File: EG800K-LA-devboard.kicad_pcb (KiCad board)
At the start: 4 copper layers, 35 x 35 mm, 49 parts, among them J1 U.FL-R-SMT_10_, J2 MICROQTJ, J5 Conn_01x08_Pin, Q1 DTC143ZUAT106, Q2 DTC143ZUAT106, Q4 DTC143ZUAT106, Q5 DTC143ZUAT106, Q6 BSS138, Q7 BSS138, Q8 BSS138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

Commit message: version final
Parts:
- removed the G*** at (151.1, 70.5)
- added G***: LOGO, Images:LOGOv3.4, F.Cu at (166.6, 88.8)
- moved J1 2.36 mm to (149.5, 65.0)
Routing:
- net /RF_ANT: track 6.12 -> 3.76 mm
- net GND: vias 729 -> 25

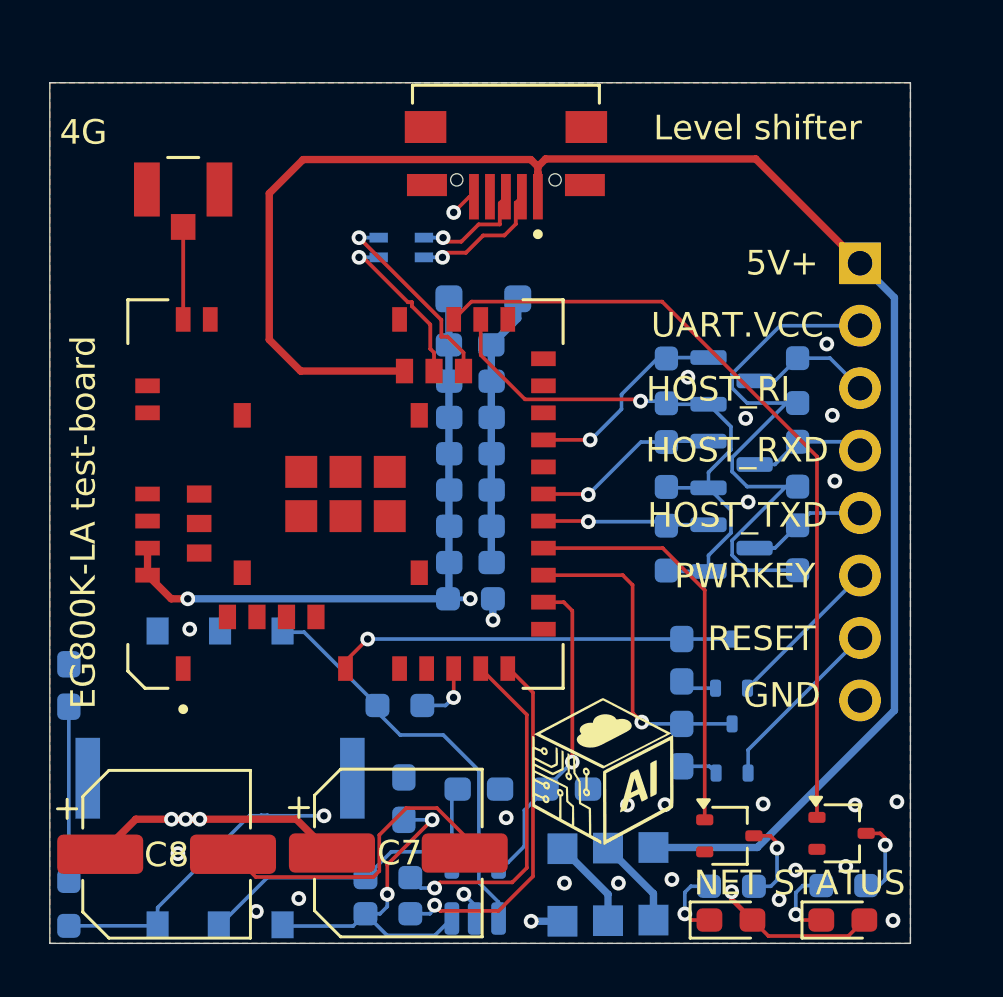
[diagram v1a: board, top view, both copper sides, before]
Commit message: cambio stack JLC PCB, cambio USB route
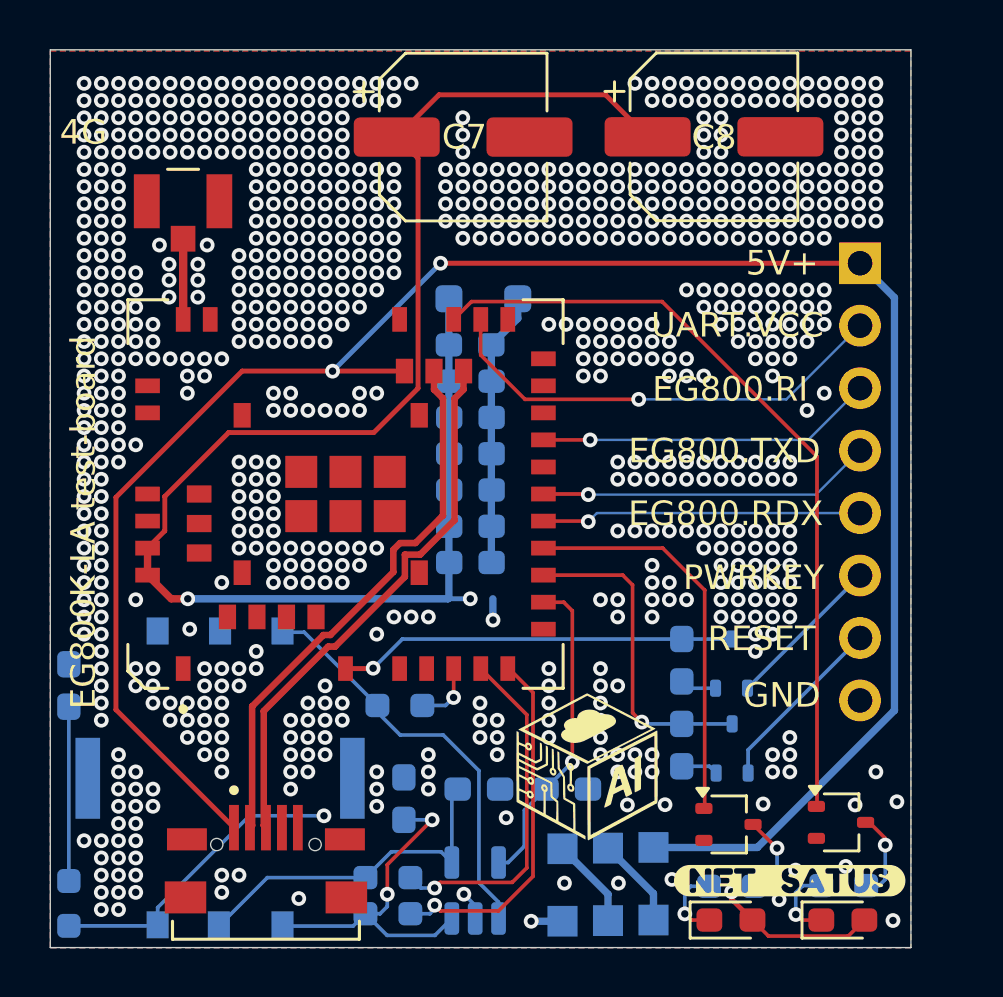
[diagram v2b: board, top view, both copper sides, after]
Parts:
- removed FL2: Choke_CommonMode_FerriteCore_1243, EasyEDA:FILTER-SMD_4P-L2.0-W1.2-BL_DLW21H
- removed Q6, Q7, Q8: BSS138, Package_TO_SOT_SMD:SOT-23
- removed R12, R13, R14, R18, R19, R20: 10k, Resistor_SMD:R_0603_1608Metric_Pad0.98x0.95mm_HandSolder
- removed R15: 0, Resistor_SMD:R_0603_1608Metric_Pad0.98x0.95mm_HandSolder
- added kibuzzard-69C732A2: G***, kibuzzard-69C732A2, F.Cu at (174.2, 93.1)
- moved C8 36.7 mm to (171.1, 62.9)
- moved C7 29.2 mm to (160.9, 62.9)
- moved J2 28.7 mm to (152.9, 91.6), turned to 0 degrees
- moved G*** 0.67 mm to (165.9, 88.6)
- moved J1 0.48 mm to (149.5, 65.5)
- moved Q5 0.46 mm to (171.7, 90.8)
- moved Q4 0.45 mm to (176.3, 90.7)
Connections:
- C21 pad 2: /EG800K.VBAT -> /DC 3.8v supply
- C22 pad 2: /EG800K.VBAT -> /DC 3.8v supply
- C23 pad 2: /EG800K.VBAT -> /DC 3.8v supply
- C24 pad 2: /EG800K.VBAT -> /DC 3.8v supply
- C25 pad 2: /EG800K.VBAT -> /DC 3.8v supply
- C26 pad 2: /EG800K.VBAT -> /DC 3.8v supply
- C27 pad 2: /EG800K.VBAT -> /DC 3.8v supply
- D5 pad 1: /EG800K.VBAT -> /DC 3.8v supply
- D6 pad 2: /EG800K.VBAT -> /DC 3.8v supply
- D7 pad 2: /EG800K.VBAT -> /DC 3.8v supply
- J2 pad 2: Net-(J2-D-) -> /EG800K.USB_D-
- J2 pad 3: Net-(J2-D+) -> /EG800K.USB_D+
- J5 pad 2: /UART.VCC -> /EG800K.VDD_ETX
- J5 pad 3: /HOST.RI_INT -> /EG800K.UART1_Ri
- J5 pad 4: /HOST_UART0_RXD -> /EG800K.UART1_TXD
- J5 pad 5: /HOST_UART0_TXD -> /EG800K.UART1_RXD
- U4 pad 42: /EG800K.VBAT -> /DC 3.8v supply
- U4 pad 43: /EG800K.VBAT -> /DC 3.8v supply
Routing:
- net /DC 3.8v supply: track 49.4 -> 127.5 mm
- net /EG800K.VBAT: track 52.1 -> 0.00 mm, vias 3 -> 0
- net /UART.VCC: track 23.7 -> 0.00 mm
- net /EG800K.USB_D-: track 6.88 -> 22.5 mm, vias 1 -> 0
- net /EG800K.USB_D+: track 8.13 -> 22.5 mm, vias 1 -> 0
- net GND: track 29.4 -> 15.4 mm, vias 25 -> 767
- net +5V: track 71.7 -> 83.4 mm, vias 0 -> 2
- net /EG800K.UART1_TXD: track 7.62 -> 14.1 mm
- net /EG800K.UART1_RXD: track 6.81 -> 13.0 mm
- net Net-(J2-D-): track 5.65 -> 0.00 mm, vias 1 -> 0
- net /EG800K.UART1_Ri: track 8.45 -> 13.8 mm
- net /HOST.RI_INT: track 5.18 -> 0.00 mm
- net /HOST_UART0_TXD: track 4.88 -> 0.00 mm
- net /HOST_UART0_RXD: track 4.82 -> 0.00 mm
- net Net-(J2-D+): track 4.81 -> 0.00 mm, vias 1 -> 0
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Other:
- board size 35 x 35 mm -> 35 x 36.5 mm
- board text added: "EG800.RDX"
- board text added: "EG800.RI"
- board text added: "EG800.TXD"
- board text removed: "HOST_RI"
- board text removed: "HOST_RXD"
- board text removed: "HOST_TXD"
- board text removed: "Level shifter"
- board text removed: "NET"
- board text removed: "STATUS"

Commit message: cambios minimos
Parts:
- added C1: 33pF, Capacitor_SMD:C_0603_1608Metric_Pad1.08x0.95mm_HandSolder, B.Cu at (181.9, 85.2)
- added C2: 33pF, Capacitor_SMD:C_0603_1608Metric_Pad1.08x0.95mm_HandSolder, B.Cu at (195.6, 89.8)
- added C21: 47uf, Capacitor_SMD:C_0603_1608Metric_Pad1.08x0.95mm_HandSolder, B.Cu at (198.3, 80.2)
- added C22: 33pf, Capacitor_SMD:C_0603_1608Metric_Pad1.08x0.95mm_HandSolder, B.Cu at (198.3, 71.3)
- added C23: 100nf, Capacitor_SMD:C_0603_1608Metric_Pad1.08x0.95mm_HandSolder, B.Cu at (198.3, 72.8)
- added C24: 10nf, Capacitor_SMD:C_0603_1608Metric_Pad1.08x0.95mm_HandSolder, B.Cu at (198.3, 74.3)
- added C25: 0.1uf, Capacitor_SMD:C_0603_1608Metric_Pad1.08x0.95mm_HandSolder, B.Cu at (198.3, 75.7)
- added C26: 1uf, Capacitor_SMD:C_0603_1608Metric_Pad1.08x0.95mm_HandSolder, B.Cu at (198.3, 77.2)
- added C27: 10uf, Capacitor_SMD:C_0603_1608Metric_Pad1.08x0.95mm_HandSolder, B.Cu at (198.3, 78.7)
- added C3: 10nf, Capacitor_SMD:C_0603_1608Metric_Pad1.08x0.95mm_HandSolder, B.Cu at (206.9, 84.1)
- added C4: 33pF, Capacitor_SMD:C_0603_1608Metric_Pad1.08x0.95mm_HandSolder, B.Cu at (198.6, 89.4)
- added C5: 100nf, Capacitor_SMD:C_0603_1608Metric_Pad1.08x0.95mm_HandSolder, B.Cu at (202.2, 89.4)
- added C6: 10nf, Capacitor_SMD:C_0603_1608Metric_Pad1.08x0.95mm_HandSolder, B.Cu at (206.9, 87.6)
- added C7: 470uF, Capacitor_SMD:CP_Elec_6.3x7.7, F.Cu at (198.0, 62.9)
- added C8: 470uF, Capacitor_SMD:CP_Elec_6.3x7.7, F.Cu at (208.2, 62.9)
- added D1: ESDA6V1SC5, Package_TO_SOT_SMD:SOT-23-5, B.Cu at (198.5, 93.5)
- added D3: KUU SS36, Snapeda:KUU_SS36_foot, B.Cu at (205.7, 93.2)
- added D4: KUU SS36, Snapeda:KUU_SS36_foot, B.Cu at (203.9, 93.3)
- added D5: SMFJ5.0A, Diode_SMD:D_SOD-123F, B.Cu at (198.8, 69.4)
- added D6: LED, LED_SMD:LED_0603_1608Metric_Pad1.05x0.95mm_HandSolder, F.Cu at (213.4, 94.7)
- added D7: LED, LED_SMD:LED_0603_1608Metric_Pad1.05x0.95mm_HandSolder, F.Cu at (208.9, 94.7)
- added D8: KUU SS36, Snapeda:KUU_SS36_foot, B.Cu at (202.0, 93.3)
- added G***: LOGO, Images:LOGOv3.4, F.Cu at (203.0, 88.6)
- added J1: U.FL-R-SMT_10_, Snapeda:U.FL-R-SMT_10_-foot, F.Cu at (186.6, 65.5)
- added J2: MICROQTJ, Snapeda:MICROQTJ-foot, F.Cu at (189.9, 91.6)
- added J5: Conn_01x08_Pin, Connector_PinHeader_2.54mm:PinHeader_1x08_P2.54mm_Vertical, B.Cu at (214.1, 68.0)
- added NANO-SIM-0501A-P1: NANO-SIM-0501A-P, Snapeda:nano-sim-0501a-p_foot, B.Cu at (188.1, 88.9)
- added Q1: DTC143ZUAT106, Package_TO_SOT_SMD:SOT-323_SC-70, B.Cu at (208.9, 84.3)
- added Q2: DTC143ZUAT106, Package_TO_SOT_SMD:SOT-323_SC-70, B.Cu at (208.9, 87.7)
- added Q4: DTC143ZUAT106, Package_TO_SOT_SMD:SOT-323_SC-70, F.Cu at (213.3, 90.7)
- added Q5: DTC143ZUAT106, Package_TO_SOT_SMD:SOT-323_SC-70, F.Cu at (208.8, 90.8)
- added R1: 0, Resistor_SMD:R_0603_1608Metric_Pad0.98x0.95mm_HandSolder, B.Cu at (194.9, 93.0)
- added R16: 2.2k, Resistor_SMD:R_0603_1608Metric_Pad0.98x0.95mm_HandSolder, B.Cu at (213.4, 93.3)
- added R17: 2.2k, Resistor_SMD:R_0603_1608Metric_Pad0.98x0.95mm_HandSolder, B.Cu at (208.9, 93.3)
- added R2: 0, Resistor_SMD:R_0603_1608Metric_Pad0.98x0.95mm_HandSolder, B.Cu at (194.9, 94.5)
- added R3: 0, Resistor_SMD:R_0603_1608Metric_Pad0.98x0.95mm_HandSolder, B.Cu at (195.4, 86.0)
- added R4: 15k, Resistor_SMD:R_0603_1608Metric_Pad0.98x0.95mm_HandSolder, B.Cu at (181.9, 94.0)
- added U4: EG800KEULC-I03-SNNSA, Snapeda:Quectel_EG800K_foot_recorted, F.Cu at (193.2, 77.4)
- added kibuzzard-69C732A2: G***, kibuzzard-69C732A2, F.Cu at (211.2, 93.1)
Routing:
- net /DC 3.8v supply: track 127.5 -> 255.1 mm, vias 5 -> 10
- net +5V: track 83.4 -> 164.1 mm, vias 2 -> 6
- net /SIM_VDD: track 37.2 -> 74.5 mm, vias 2 -> 4
- net /EG800K.STATUS: track 31.9 -> 63.9 mm
- net /EG800K.USB_D+: track 22.5 -> 45.0 mm
- net /EG800K.USB_D-: track 22.5 -> 45.0 mm
- net /EG800K.VDD_ETX: track 18.9 -> 37.7 mm, vias 1 -> 2
- net Net-(NANO-SIM-0501A-P1-I/O): track 16.8 -> 33.6 mm
- net /EG800K.PWRKEY: track 16.2 -> 32.4 mm, vias 1 -> 2
- net /EG800K.NET_STATUS: track 16.2 -> 32.3 mm
- net GND: track 15.4 -> 30.7 mm, vias 767 -> 1612
- net /SIM_CLK: track 14.8 -> 29.6 mm, vias 1 -> 2
- net Net-(NANO-SIM-0501A-P1-CLK): track 14.2 -> 28.4 mm, vias 2 -> 4
- net /EG800K.UART1_TXD: track 14.1 -> 28.3 mm, vias 1 -> 2
- net /SIM_RST: track 14.1 -> 28.3 mm, vias 1 -> 2
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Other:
- board size 35 x 36.5 mm -> 72 x 36.5 mm
- board text added: "V_EXT 1.8v"
- board text added: "no tapered RF 0.3424 clear 0.5080 Coplanar Single Ended"
- board text added: "tapered RF 0.3424 clear 0.5080 Coplanar Single Ended"
- board text removed: "UART.VCC"

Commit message: original rediseñado
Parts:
- removed the C1 at (181.9, 85.2)
- removed the C2 at (195.6, 89.8)
- removed C21: 47uf, Capacitor_SMD:C_0603_1608Metric_Pad1.08x0.95mm_HandSolder
- removed C22: 33pf, Capacitor_SMD:C_0603_1608Metric_Pad1.08x0.95mm_HandSolder
- removed C23: 100nf, Capacitor_SMD:C_0603_1608Metric_Pad1.08x0.95mm_HandSolder
- removed C24: 10nf, Capacitor_SMD:C_0603_1608Metric_Pad1.08x0.95mm_HandSolder
- removed C25: 0.1uf, Capacitor_SMD:C_0603_1608Metric_Pad1.08x0.95mm_HandSolder
- removed C26: 1uf, Capacitor_SMD:C_0603_1608Metric_Pad1.08x0.95mm_HandSolder
- removed C27: 10uf, Capacitor_SMD:C_0603_1608Metric_Pad1.08x0.95mm_HandSolder
- removed the C3 at (206.9, 84.1)
- removed the C4 at (198.6, 89.4)
- removed the C5 at (202.2, 89.4)
- removed the C6 at (206.9, 87.6)
- removed the C7 at (198.0, 62.9)
- removed the C8 at (208.2, 62.9)
- removed the D1 at (198.5, 93.5)
- removed the D3 at (205.7, 93.2)
- removed the D4 at (203.9, 93.3)
- removed the D5 at (198.8, 69.4)
- removed the D6 at (213.4, 94.7)
- removed the D7 at (208.9, 94.7)
- removed D8: KUU SS36, Snapeda:KUU_SS36_foot
- removed G*** (x2): LOGO, Images:LOGOv3.4
- removed the J1 at (186.6, 65.5)
- removed the J2 at (189.9, 91.6)
- removed J5 (x2): Conn_01x08_Pin, Connector_PinHeader_2.54mm:PinHeader_1x08_P2.54mm_Vertical
- removed the NANO-SIM-0501A-P1 at (188.1, 88.9)
- removed the Q1 at (208.9, 84.3)
- removed the Q2 at (208.9, 87.7)
- removed the Q4 at (213.3, 90.7)
- removed the Q5 at (208.8, 90.8)
- removed the R1 at (194.9, 93.0)
- removed R16, R17: 2.2k, Resistor_SMD:R_0603_1608Metric_Pad0.98x0.95mm_HandSolder
- removed the R2 at (194.9, 94.5)
- removed the R3 at (195.4, 86.0)
- removed the R4 at (181.9, 94.0)
- removed U4 (x2): EG800KEULC-I03-SNNSA, Snapeda:Quectel_EG800K_foot_recorted
- removed kibuzzard-69C732A2 (x2): G***, kibuzzard-69C732A2
- added BAT+1: BAT+, Connector_Wire:SolderWirePad_1x01_SMD_2x4mm, B.Cu at (151.0, 92.8)
- added BAT-1: BAT-, Connector_Wire:SolderWirePad_1x01_SMD_2x4mm, B.Cu at (147.5, 92.8)
- added J3: Conn_01x09_Pin, Connector_PinHeader_2.54mm:PinHeader_1x09_P2.54mm_Vertical, B.Cu at (145.5, 86.5)
- added Q3: AO3415, Package_TO_SOT_SMD:SOT-23, B.Cu at (158.1, 89.5)
- added R5: 2.4K, Resistor_SMD:R_0603_1608Metric_Pad0.98x0.95mm_HandSolder, B.Cu at (158.2, 92.3)
- added R6: 10k, Resistor_SMD:R_0603_1608Metric_Pad0.98x0.95mm_HandSolder, B.Cu at (158.2, 94.1)
- added U1: EG800KEULC-I03-SNNSA, Snapeda:Quectel_EG800K_foot_recorted, F.Cu at (166.9, 75.4)
- added U2: TP4057, Package_TO_SOT_SMD:TSOT-23-6, B.Cu at (161.9, 92.0)
- added kibuzzard-6A166AE0: G***, kibuzzard-6A166AE0, F.Cu at (146.3, 63.5)
- added kibuzzard-6A166AEF: G***, kibuzzard-6A166AEF, F.Cu at (153.7, 63.5)
- C10: renamed from C22; moved to F.Cu
- C11: renamed from C23; moved to F.Cu
- C12: renamed from C24; moved to F.Cu
- C13: renamed from C25; moved to F.Cu
- C14: renamed from C26; moved to F.Cu
- C15: renamed from C27; moved to F.Cu
- C9: renamed from C21; moved to F.Cu
- D2: renamed from D3; moved to F.Cu
- D3: renamed from D4; moved to F.Cu
- D4: renamed from D8; moved to F.Cu
- R7: renamed from R16; moved to F.Cu
- R8: renamed from R17; moved to F.Cu
- moved R8 41.9 mm to (146.1, 60.3)
- moved D7 41.8 mm to (146.1, 61.8)
- moved R7 40.7 mm to (152.5, 60.3)
- moved D6 40.6 mm to (152.5, 61.8)
- moved Q5 37.4 mm to (149.1, 61.0), turned to -90 degrees
- moved C7 36.7 mm to (149.0, 92.2)
- moved Q4 36.2 mm to (155.5, 61.0), turned to -90 degrees
- moved C2 30.5 mm to (149.2, 60.8), turned to 0 degrees
- moved C4 29.9 mm to (149.2, 64.1), turned to 0 degrees
- moved C3 29.6 mm to (149.2, 62.4), turned to 0 degrees
- moved C8 29.4 mm to (158.6, 92.1)
- moved D1 25.3 mm to (150.9, 70.6)
- moved J1 24.9 mm to (174.0, 61.2)
- moved NANO-SIM-0501A-P1 24.8 mm to (161.2, 66.3), turned to 0 degrees
- moved Q2 21.5 mm to (150.4, 86.2), turned to -90 degrees
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- renumbered C4 to C3, C5 to C4, C3 to C5, C8 to C7, C7 to C8
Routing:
- net /DC 3.8v supply: track 255.1 -> 108.7 mm, vias 10 -> 4
- net +5V: track 164.1 -> 73.4 mm, vias 6 -> 1
- net /EG800K.STATUS: track 63.9 -> 27.2 mm, vias 0 -> 2
- net /EG800K.USB_D+: track 45.0 -> 13.9 mm
- net /EG800K.USB_D-: track 45.0 -> 14.7 mm
- net GND: track 30.7 -> 1.03 mm, vias 1612 -> 363
- net +4.2V: track 0.00 -> 25.9 mm, vias 0 -> 2
- net Net-(NANO-SIM-0501A-P1-I/O): track 33.6 -> 10.6 mm
- net /SIM_VDD: track 74.5 -> 52.4 mm, vias 4 -> 3
- net /SIM_CLK: track 29.6 -> 9.84 mm, vias 2 -> 1
- net /SIM_RST: track 28.3 -> 10.0 mm, vias 2 -> 1
- net /EG800K.PWRKEY: track 32.4 -> 14.8 mm
- net /EG800K.RESET: track 26.5 -> 15.8 mm
- net /HOST.EG800K.RESET: track 14.8 -> 8.35 mm, vias 0 -> 2
- net /HOST.EG800K.PWRKEY: track 13.0 -> 7.35 mm, vias 0 -> 2
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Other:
- board size 72 x 36.5 mm -> 35 x 36.5 mm
- board text added: "BAT out"
- board text removed: "10K.FET.10K"
- board text removed: "4G"
- board text removed: "Luis D."
- board text removed: "R0"
- board text removed: "no tapered RF 0.3424 clear 0.5080 Coplanar Single Ended"
